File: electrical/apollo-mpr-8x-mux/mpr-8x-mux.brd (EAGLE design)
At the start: 100 x 100 mm, 30 parts, among them IC1 LM1117-3V3, Q1 2N7002D, Q2 2N7002D, U2 MCP23017SS, X1 RJ45-8-2-CONEC-1, X2 RJ45-8-2-CONEC-1, X3 RJ45-8-2-CONEC-1, X4 RJ45-8-2-CONEC-1, X5 RJ45-8-2-CONEC-1, X6 RJ45-8-2-CONEC-1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

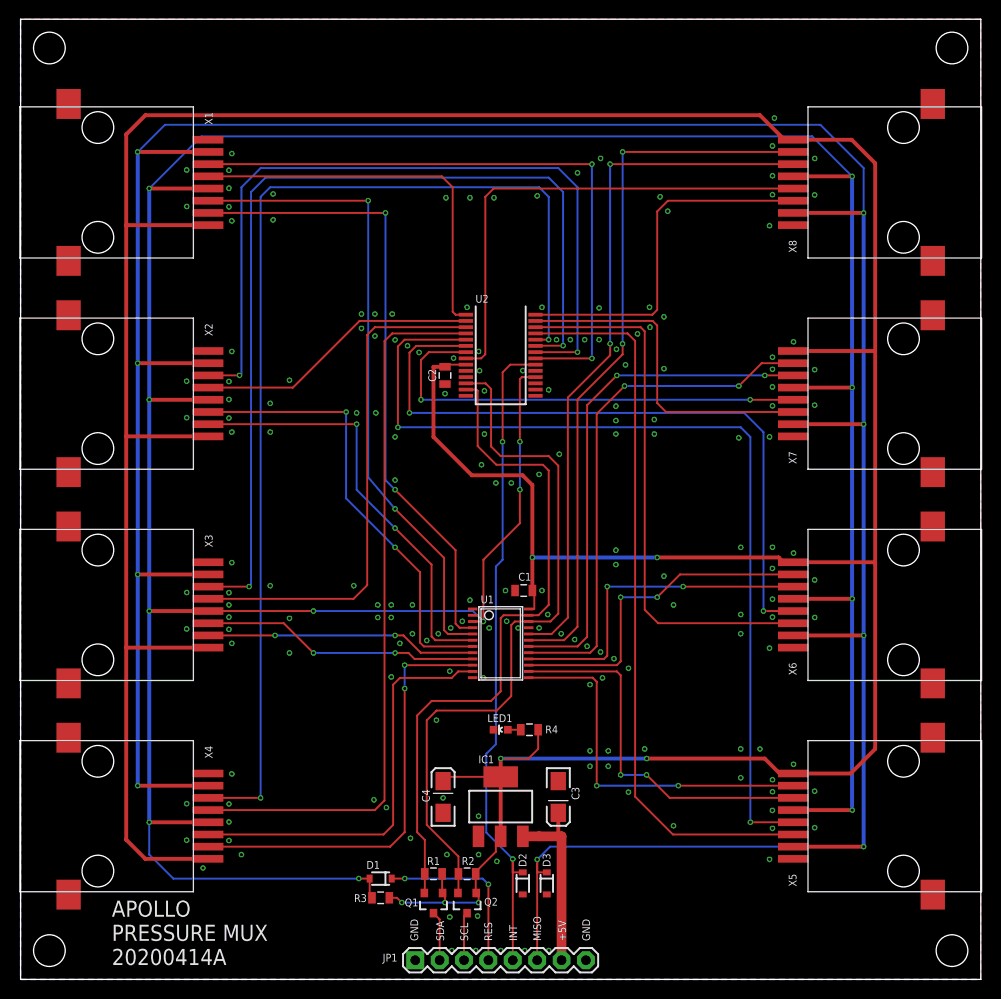
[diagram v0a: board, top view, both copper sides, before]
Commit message: fixed chip select problem with mosfets
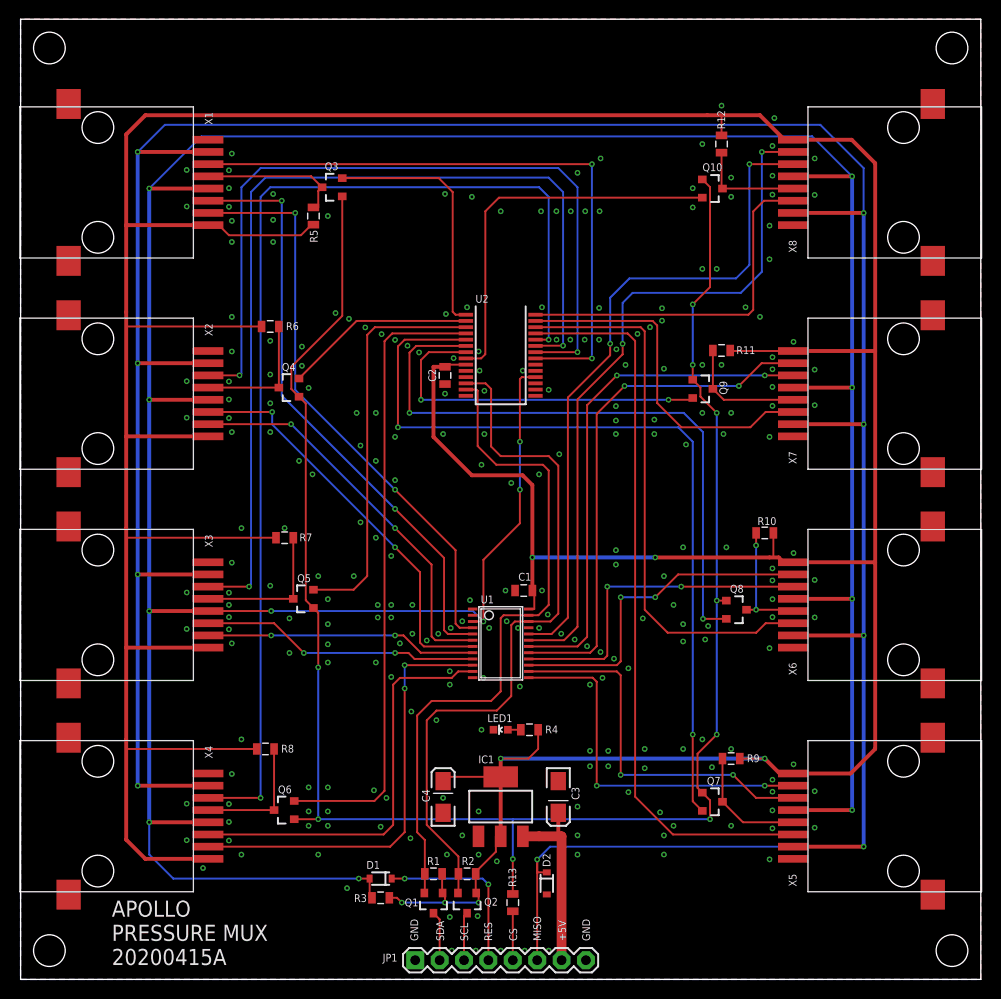
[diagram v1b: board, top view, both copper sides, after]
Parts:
- removed D3: 3V6, apollo-ctrl:SOD-323
- added Q10, Q3, Q4, Q5, Q6, Q7, Q8, Q9: 2N7002D, apollo-ctrl:SOT23-3
- added R10, R11, R12, R5, R6, R7, R8, R9: 4K7, apollo-ctrl:0805
- added R13: 470R, apollo-ctrl:0805
- moved D2 2.50 mm to (54.8, 10.0)
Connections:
- removed net INT: D2.1, JP1.5, U2.20
- new net CS-MASTER: Q10.1, Q3.1, Q4.1, Q5.1, Q6.1, Q7.1, Q8.1, Q9.1, R13.1
- new net N$10: JP1.5, R13.2
- new net N$2: Q7.3, R9.1, X5.5
- new net N$3: Q8.3, R10.1, X6.5
- new net N$4: Q9.3, R11.1, X7.5
- new net N$5: Q10.3, R12.1, X8.5
- new net N$6: Q6.3, R8.1, X4.5
- new net N$7: Q5.3, R7.1, X3.5
- new net N$8: Q4.3, R6.1, X2.5
- new net N$9: Q3.3, R5.1, X1.5
- net 3.3V: now also R10.2, R11.2, R12.2, R5.2, R6.2, R7.2, R8.2, R9.2
- net CS1: now also Q3.2; no longer X1.5
- net CS2: now also Q4.2; no longer X2.5
- net CS3: now also Q5.2; no longer X3.5
- net CS4: now also Q6.2; no longer X4.5
- net CS5: now also Q7.2; no longer X5.5
- net CS6: now also Q8.2; no longer X6.5
- net CS7: now also Q9.2; no longer X7.5
- net CS8: now also Q10.2; no longer X8.5
- net GND: no longer D3.2
- net MISO: now also D2.1; no longer D3.1
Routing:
- net CS-MASTER: track 0.00 -> 190.4 mm, vias 0 -> 9
- net 3.3V: track 414.6 -> 489.0 mm
- net INT: track 69.3 -> 0.00 mm, vias 2 -> 0
- net N$7: track 0.00 -> 15.2 mm
- net N$9: track 0.00 -> 15.1 mm
- net CS1: track 40.4 -> 26.1 mm
- net N$8: track 0.00 -> 13.7 mm
- net N$6: track 0.00 -> 13.2 mm
- net N$3: track 0.00 -> 13.0 mm, vias 0 -> 2
- net N$4: track 0.00 -> 12.9 mm
- net N$2: track 0.00 -> 12.8 mm
- net CS3: track 53.8 -> 41.9 mm
- net CS5: track 97.5 -> 86.0 mm
- net N$5: track 0.00 -> 11.2 mm
- net CS8: track 51.0 -> 40.3 mm
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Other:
- board text added: "APOLLO PRESSURE MUX 20200415A"
- board text added: "CS"
- board text removed: "APOLLO PRESSURE MUX 20200414A"
- board text removed: "INT"

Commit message: added 2x4 header to mpr-8x-mux pcb
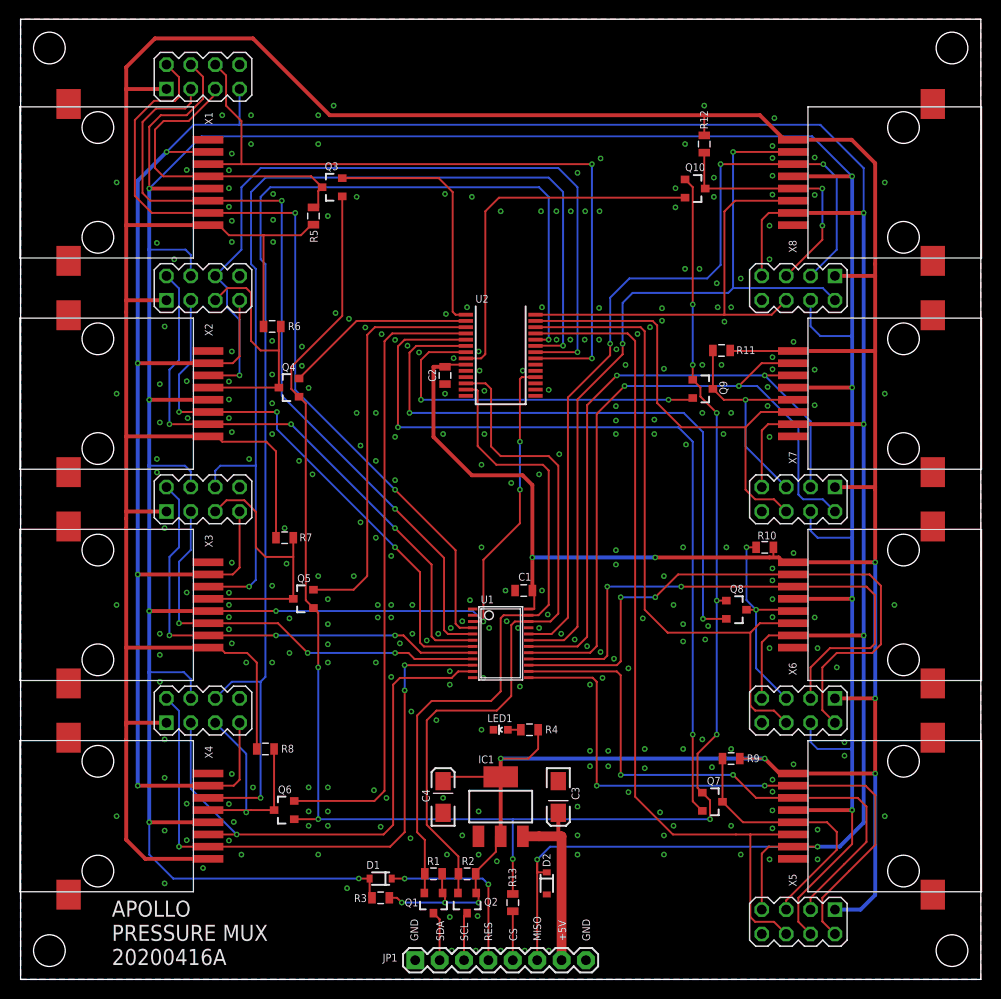
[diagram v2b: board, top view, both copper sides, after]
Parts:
- added X10, X11, X12, X13, X14, X15, X16, X9: TP-GROUP-X8-2X04, apollo-ctrl:2X4
- moved Q10 1.80 mm to (70.2, 82.4)
- moved R12 1.80 mm to (71.2, 87.0)
- moved R10 1.50 mm to (77.5, 45.0)
- moved R6 0.20 mm to (26.2, 68.0)
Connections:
- net 3.3V: now also X10.1, X11.1, X12.1, X13.1, X14.1, X15.1, X16.1, X9.1
- net EOC1: now also X9.6
- net EOC2: now also X10.6
- net EOC3: now also X11.6
- net EOC4: now also X12.6
- net EOC5: now also X13.6
- net EOC6: now also X14.6
- net EOC7: now also X15.6
- net EOC8: now also X16.6
- net GND: now also X10.8, X11.8, X12.8, X13.8, X14.8, X15.8, X16.8, X9.8
- net MISO: now also X10.7, X11.7, X12.7, X13.7, X14.7, X15.7, X16.7, X9.7
- net N$2: now also X13.5
- net N$3: now also X14.5
- net N$4: now also X15.5
- net N$5: now also X16.5
- net N$6: now also X12.5
- net N$7: now also X11.5
- net N$8: now also X10.5
- net N$9: now also X9.5
- net RES: now also X10.4, X11.4, X12.4, X13.4, X14.4, X15.4, X16.4, X9.4
- net SCL1: now also X9.3
- net SCL2: now also X10.3
- net SCL3: now also X11.3
- net SCL4: now also X12.3
- net SCL5: now also X13.3
- net SCL6: now also X14.3
- net SCL7: now also X15.3
- net SCL8: now also X16.3
- net SDA1: now also X9.2
- net SDA2: now also X10.2
- net SDA3: now also X11.2
- net SDA4: now also X12.2
- net SDA5: now also X13.2
- net SDA6: now also X14.2
- net SDA7: now also X15.2
- net SDA8: now also X16.2
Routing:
- net 3.3V: track 489.0 -> 583.4 mm, vias 7 -> 10
- net RES: track 346.5 -> 419.8 mm
- net MISO: track 321.6 -> 380.3 mm
- net SDA6: track 35.4 -> 64.5 mm
- net SDA5: track 38.6 -> 64.8 mm
- net SDA1: track 60.7 -> 86.5 mm
- net SCL6: track 34.9 -> 59.8 mm
- net SCL1: track 62.5 -> 84.4 mm
- net SCL5: track 39.1 -> 60.2 mm
- net SDA3: track 28.3 -> 48.7 mm, vias 2 -> 3
- net SDA2: track 41.3 -> 61.7 mm, vias 2 -> 3
- net SDA7: track 54.2 -> 73.8 mm
- net SDA4: track 45.6 -> 64.6 mm, vias 2 -> 3
- net N$9: track 15.1 -> 33.3 mm
- net SCL8: track 70.9 -> 87.4 mm, vias 2 -> 3
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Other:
- board text added: "APOLLO PRESSURE MUX 20200416A"
- board text removed: "APOLLO PRESSURE MUX 20200415A"
